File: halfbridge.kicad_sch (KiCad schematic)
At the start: 43 parts, among them Q5 Q_NIGBT_GCE, Q6 Q_NIGBT_GCE, U10 ADuM121N, U13 EL7202CN, U14 EL7202CN, U17 ACS730xLCTR-50AB, U9 ADuM121N

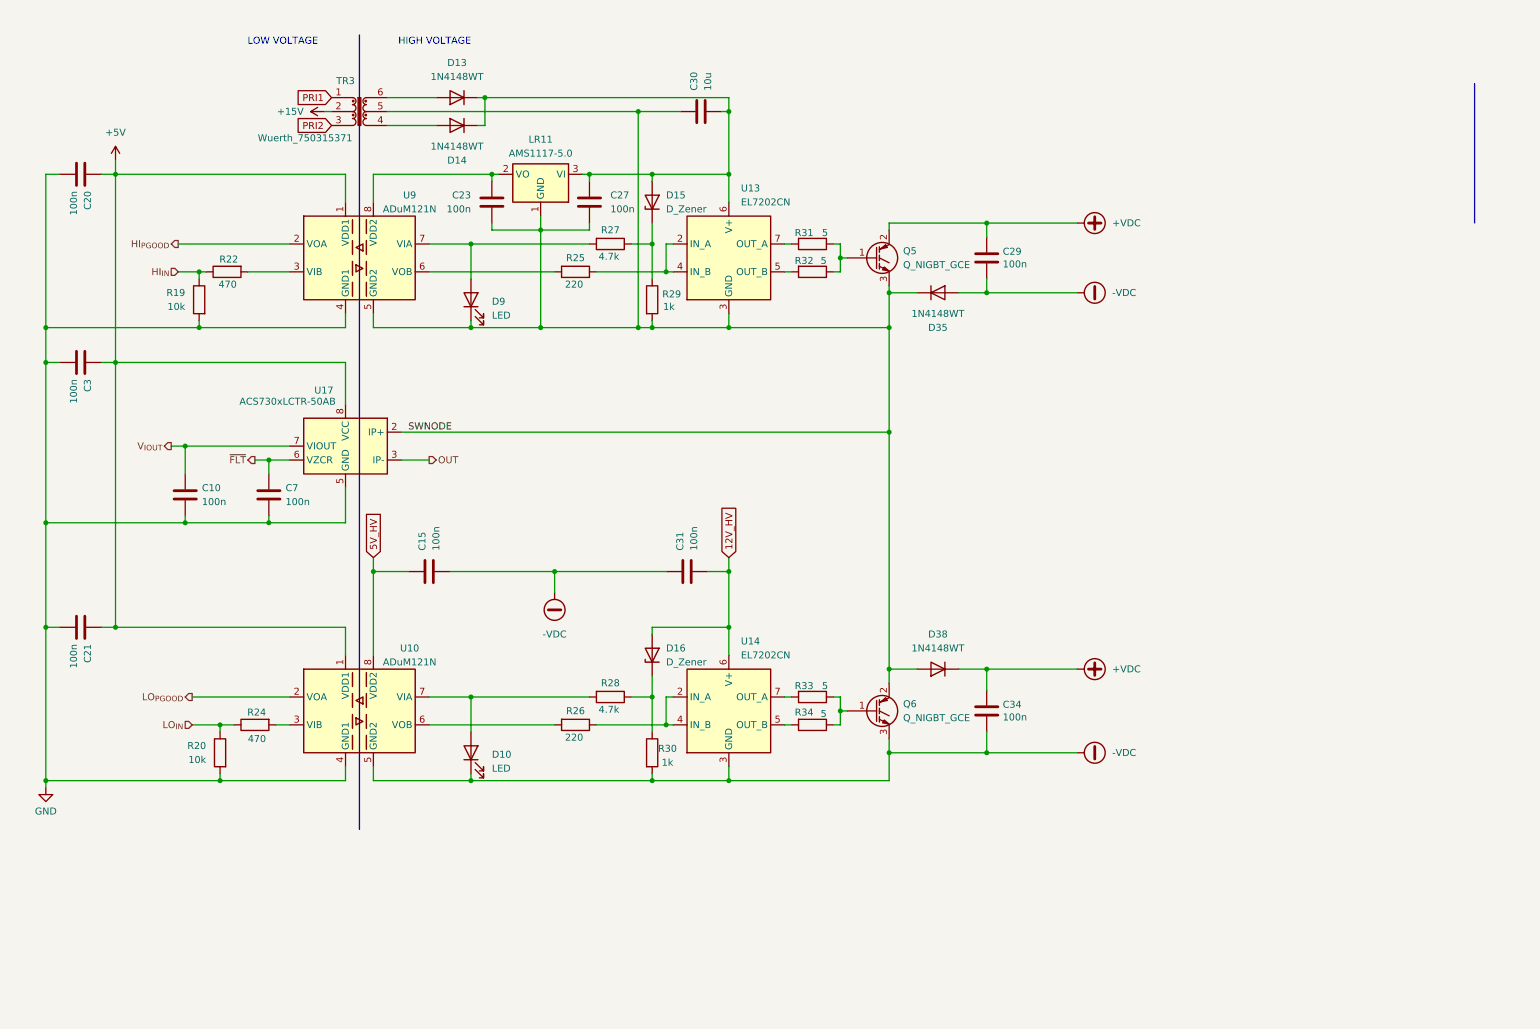
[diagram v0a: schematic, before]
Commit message: Updated LDO footrprint to use the SOT89 LM78L05 (issue 10); moved high side local regulators closer to digital isolator ICs (issue 10); pushed digital isolator ICs further to the allow room for LRs (issue 10); changed designator letter for zener diodes to Z to make it easier when hand soldering (issue 5) Updated footprints from placeholders (most of the diodes) to actual real component choices updated resistor values for BOM consolidation (220, 1k) moved resistor related to PGOOD for more optimal routing w/ minimal impact to function Changed structure of isolated driver design to use voltage doubler and 6505 or similar IC directly (issue 7,8,13) Only 5VDC is required for low voltage side, although several amps may be required depending on gate drive requirements Updated transformer footprint for more common 7.5mm by 2.5mm spacing, several 1:1.1 to 1:1.5 transformers are avilable with such spacing (issue 7) Moved Q8 designator back to correct place along with others that were mislocated somehow... Fixed placement of some footprints that were slightly off or not aligned to 0.25mm grid Replaced specific SO8 MOSFET driver with choose-your-own generic. I am personally using some cheapo LCSC TI 27523 clones (issue 11) added EVEN MORE VIAS!!!! thermal vias on not current sensitive pins to make soldering easier Added artwork (issue 6)
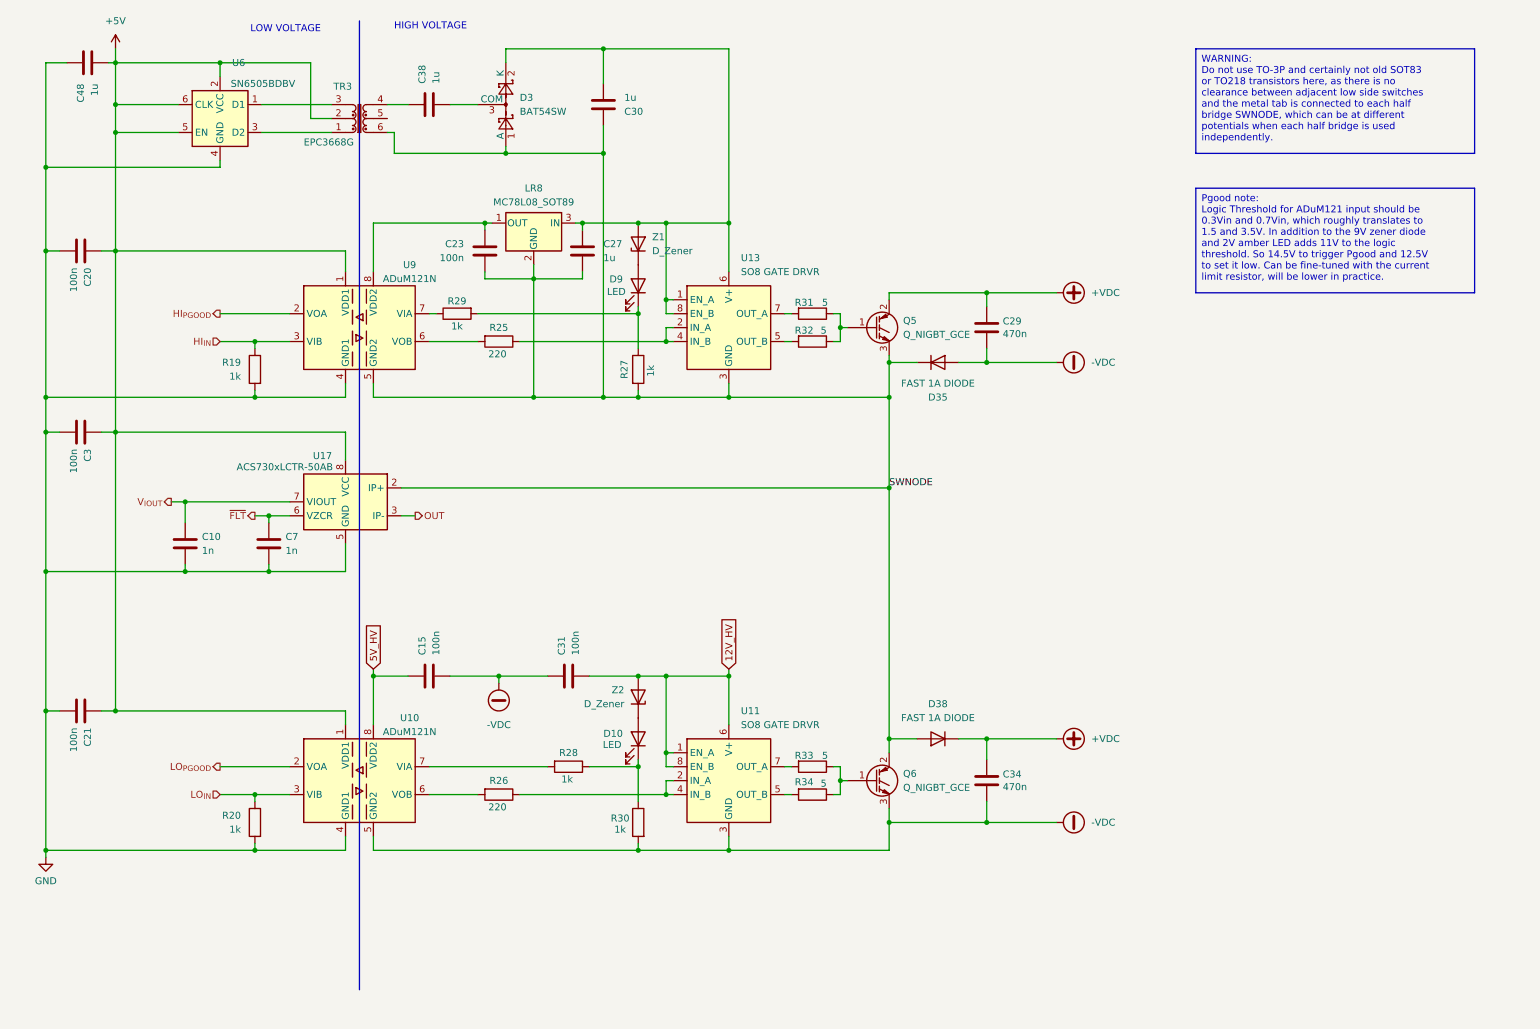
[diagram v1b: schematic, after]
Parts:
- removed D13, D14: 1N4148WT, Diode_SMD:D_SOD-128, symbol Diode:1N4148WT
- removed LR11: AMS1117-5.0, Package_TO_SOT_SMD:SOT-89-3, symbol Regulator_Linear:AMS1117-5.0
- removed R22, R24: 470, Resistor_SMD:R_0603_1608Metric, symbol Device:R
- removed U14: EL7202CN, Package_SO:SO-8_3.9x4.9mm_P1.27mm, symbol Driver_FET:EL7202CN
- added C38, C48: 1u, Capacitor_SMD:C_0603_1608Metric, symbol Device:C
- added D3: BAT54SW, Package_TO_SOT_SMD:SOT-323_SC-70, symbol Diode:BAT54SW
- added LR8: MC78L08_SOT89, Package_TO_SOT_SMD:SOT-89-3, symbol Regulator_Linear:MC78L08_SOT89
- added U11: SO8 GATE DRVR, Package_SO:SO-8_3.9x4.9mm_P1.27mm, symbol Driver_FET:EL7202CN
- added U6: SN6505BDBV, Package_TO_SOT_SMD:SOT-23-6, symbol Power_Management:SN6505BDBV
- C10, C7: value 100n -> 1n
- C27: value 100n -> 1u
- C29, C34: value 100n -> 470n
- C30: value 10u -> 1u; footprint Capacitor_SMD:C_0805_2012Metric -> Capacitor_SMD:C_0603_1608Metric
- D10: footprint LED_SMD:LED_0603_1608Metric -> LED_SMD:LED_0805_2012Metric
- D35, D38: value 1N4148WT -> FAST 1A DIODE
- D9: footprint LED_SMD:LED_0603_1608Metric -> Capacitor_SMD:C_0805_2012Metric
- R19, R20: value 10k -> 1k
- R27, R28: value 4.7k -> 1k
- TR3: value Wuerth_750315371 -> EPC3668G; footprint Transformer_SMD:Transformer_Wuerth_750315371 -> Transformer_SMD:Pulse_PA2004NL
- U13: value EL7202CN -> SO8 GATE DRVR
- Z1: renamed from D15; footprint Diode_SMD:D_0603_1608Metric -> Diode_SMD:D_SOD-123
- Z2: renamed from D16; footprint Diode_SMD:D_0603_1608Metric -> Diode_SMD:D_SOD-123
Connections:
- net +15V is gone; now on net +5V: TR3.2
- net +5V: now also C48.2, U6.2 (VCC), U6.5 (EN), U6.6 (CLK)
- net -VDC: now also U11.3 (GND); no longer D10.1 (K)
- net 12V_HV: now also U11.1 (EN_A), U11.6 (V+), U11.8 (EN_B)
- net GND: now also C48.1, U6.4 (GND)
- net HI_{IN}: now also U9.3 (VIB)
- net LO_{IN}: now also U10.3 (VIB)
- net SWNODE: now also R27.2, TR3.6, D3.1 (A), LR8.2 (GND); no longer D9.1 (K), R29.2, TR3.5
- net at R28.1, R30.1: now also D10.1 (K); no longer Z2.1 (K)
- net at R28.2, U10.7 (VIA): no longer D10.2 (A)
- net at R26.1: now also U11.2 (IN_A), U11.4 (IN_B)
- net at C23.1, U9.8 (VDD2): now also LR8.1 (OUT)
- net at C27.1, C30.2, U13.6 (V+)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: now also U13.1 (EN_A), U13.8 (EN_B), D3.2 (K), LR8.3 (IN)
- net at R34.2: now also U11.5 (OUT_B)
- net at R33.2: now also U11.7 (OUT_A)
- net at TR3.4: now also C38.1
- net PRI1: no longer names the net of TR3.1
- net PRI1: now also U6.3 (D2)
- net PRI2: no longer names the net of TR3.3
- net PRI2: now also U6.1 (D1)
- new net: C38.2, D3.3 (COM)
- new net: D9.1 (K), R27.1, R29.2
- new net: R29.1, U9.7 (VIA)
- new net: D10.2 (A), Z2.1 (K)
- new net: D9.2 (A), Z1.1 (K)
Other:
- moved on the sheet: C10, C15, C20, C21, C23, C27, C29, C3, C30, C31, C34, C7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

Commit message: forgot to save and close prior to last commit
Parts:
- renumbered C38 to C39, C48 to C50, LR8 to LR11, U11 to U12
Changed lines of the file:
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@@
 		(on_board yes)
 		(dnp no)
-		(property "Reference" "C48"
+		(property "Reference" "C50"
 			(at 25.3999 25.4 0)
 			(effects
@@
 		(on_board yes)
 		(dnp no)
-		(property "Reference" "C38"
+		(property "Reference" "C39"
 			(at 87.6299 25.4 0)
 			(effects
@@
 		(dnp no)
 		(fields_autoplaced yes)
-		(property "Reference" "U11"
+		(property "Reference" "U12"
 			(at 145.7041 139.7 0)
 			(effects
@@
 		(on_board yes)
 		(dnp no)
-		(property "Reference" "LR8"
+		(property "Reference" "LR11"
 			(at 107.95 44.45 0)
 			(effects

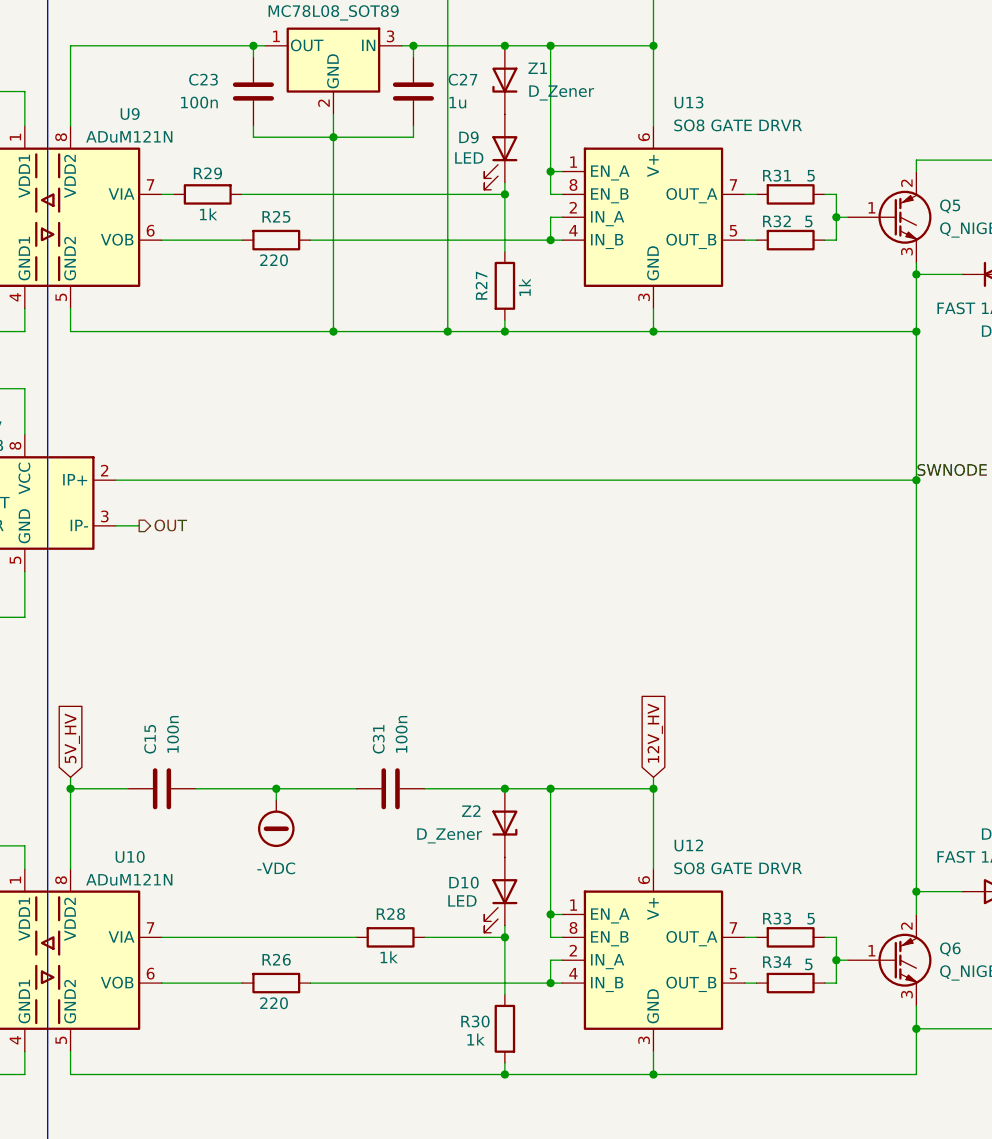
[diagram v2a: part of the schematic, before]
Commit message: fixed the accidentally flipped terminal block posistive terminal
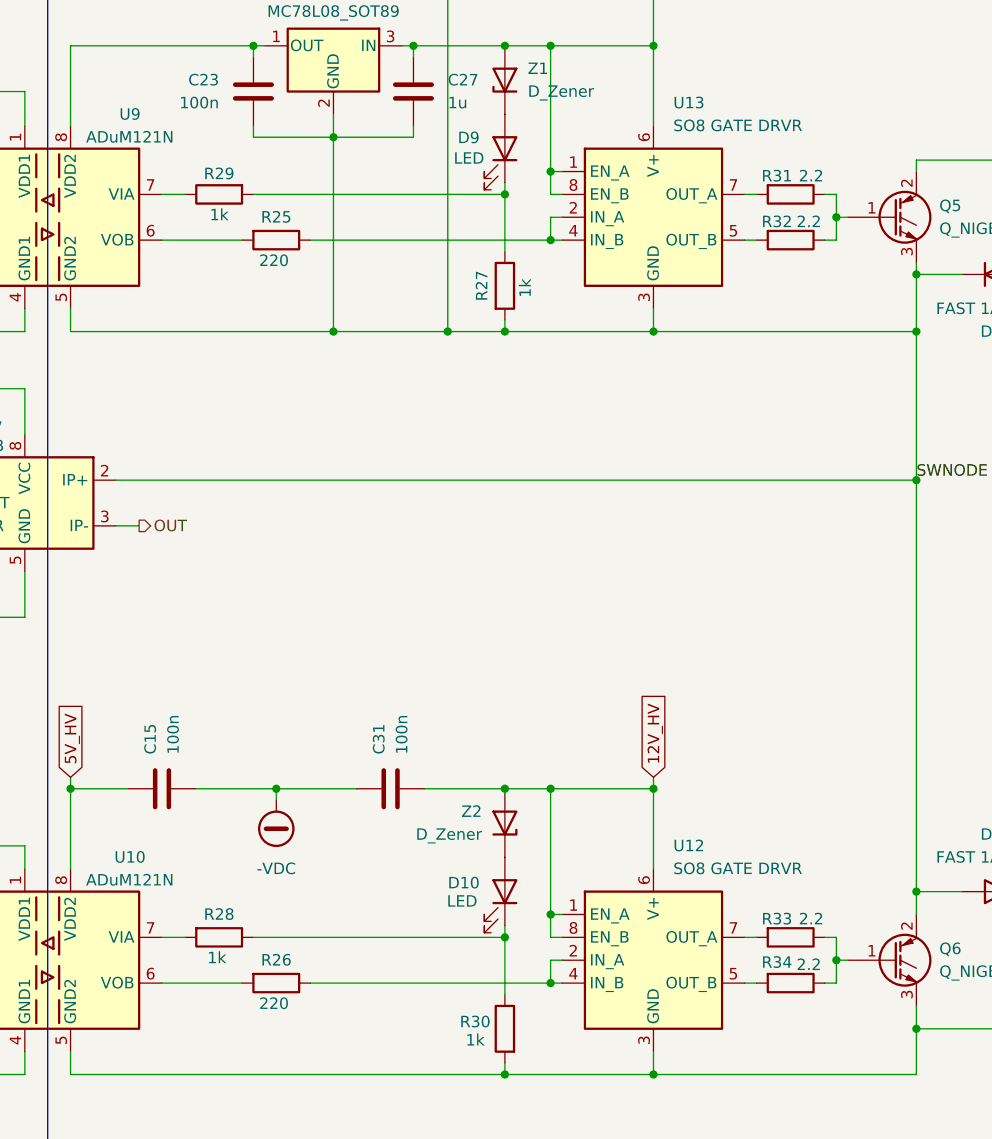
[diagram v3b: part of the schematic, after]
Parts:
- R31, R32, R33, R34: value 5 -> 2.2
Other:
- moved on the sheet: R28, R29
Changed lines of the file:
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@@
 	(wire
 		(pts
-			(xy 88.9 149.86) (xy 110.49 149.86)
+			(xy 88.9 149.86) (xy 91.44 149.86)
 		)
 		(stroke
@@
 	(wire
 		(pts
-			(xy 88.9 67.31) (xy 90.17 67.31)
+			(xy 88.9 67.31) (xy 91.44 67.31)
 		)
 		(stroke
@@
 	(wire
 		(pts
-			(xy 118.11 149.86) (xy 127 149.86)
+			(xy 99.06 149.86) (xy 127 149.86)
 		)
 		(stroke
@@
 	(wire
 		(pts
-			(xy 97.79 67.31) (xy 127 67.31)
+			(xy 99.06 67.31) (xy 127 67.31)
 		)
 		(stroke
@@
 			)
 		)
-		(property "Value" "5"
+		(property "Value" "2.2"
 			(at 161.036 65.278 90)
 			(effects
@@
 	(symbol
 		(lib_id "Device:R")
-		(at 114.3 149.86 270)
+		(at 95.25 149.86 270)
 		(unit 1)
 		(exclude_from_sim no)
@@
 		(dnp no)
 		(property "Reference" "R28"
-			(at 114.3 147.32 90)
+			(at 95.25 147.32 90)
 			(effects
 				(font
@@
 		)
 		(property "Value" "1k"
-			(at 114.046 152.146 90)
+			(at 94.996 152.146 90)
 			(effects
 				(font
@@
 		)
 		(property "Footprint" "Resistor_SMD:R_0603_1608Metric"
-			(at 114.3 148.082 90)
+			(at 95.25 148.082 90)
 			(effects
 				(font
@@
 		)
 		(property "Datasheet" "~"
-			(at 114.3 149.86 0)
+			(at 95.25 149.86 0)
 			(effects
 				(font
@@
 		)
 		(property "Description" ""
-			(at 114.3 149.86 0)
+			(at 95.25 149.86 0)
 			(effects
 				(font
@@
 	(symbol
 		(lib_id "Device:R")
-		(at 93.98 67.31 90)
+		(at 95.25 67.31 90)
 		(mirror x)
 		(unit 1)
@@
 		(dnp no)
 		(property "Reference" "R29"
-			(at 93.98 65.024 90)
+			(at 95.25 65.024 90)
 			(effects
 				(font
@@
 		)
 		(property "Value" "1k"
-			(at 93.98 69.596 90)
+			(at 95.25 69.596 90)
 			(effects
 				(font
@@
 		)
 		(property "Footprint" "Resistor_SMD:R_0603_1608Metric"
-			(at 93.98 65.532 90)
+			(at 95.25 65.532 90)
 			(effects
 				(font
@@
 		)
 		(property "Datasheet" "~"
-			(at 93.98 67.31 0)
+			(at 95.25 67.31 0)
 			(effects
 				(font
@@
 		)
 		(property "Description" ""
-			(at 93.98 67.31 0)
+			(at 95.25 67.31 0)
 			(effects
 				(font
@@
 			)
 		)
-		(property "Value" "5"
+		(property "Value" "2.2"
 			(at 160.782 70.358 90)
 			(effects
@@
 			)
 		)
-		(property "Value" "5"
+		(property "Value" "2.2"
 			(at 160.782 152.908 90)
 			(effects
@@
 			)
 		)
-		(property "Value" "5"
+		(property "Value" "2.2"
 			(at 161.036 147.828 90)
 			(effects
